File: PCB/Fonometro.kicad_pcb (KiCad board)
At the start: 2 copper layers, 120 x 120 mm, 58 parts, among them J1 Conn_01x15_Male, J2 Conn_01x15_Male, J3 Power, U1 LM324, U2 LM358, U3 ESP32-DEVKIT-V1

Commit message: feat: improved PCB layout.
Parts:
- added G***: LOGO, Logos:Jugg, F.Cu at (161.3, 127.0)
- added G***: LOGO, Logos:UniCT, F.Cu at (147.3, 127.0)
- moved R22 51.7 mm to (106.7, 120.6), turned to 90 degrees
- moved R23 41.6 mm to (124.5, 113.0), turned to -90 degrees
- moved U1 41.3 mm to (111.8, 104.1), turned to 0 degrees
- moved R21 36.9 mm to (106.7, 110.5)
- moved D2 36.9 mm to (177.8, 101.6), turned to 180 degrees
- moved D1 35.8 mm to (170.2, 106.7), turned to 0 degrees
- moved D4 29.5 mm to (177.8, 91.4), turned to 180 degrees
- moved R24 28.2 mm to (124.5, 101.6), turned to -90 degrees
- moved D3 24.1 mm to (170.2, 96.5), turned to 0 degrees
- moved R29 14.0 mm to (133.3, 68.6)
- moved J3 11.3 mm to (188.0, 79.5), turned to 120 degrees
- moved R30 11.2 mm to (121.1, 59.3), turned to 35 degrees
- moved U2 10.9 mm to (133.4, 62.2)
- moved C3 8.89 mm to (189.2, 116.8)
- moved R5 8.89 mm to (189.2, 110.5)
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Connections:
- R22 pad 1: Net-(R18-Pad2) -> MIC 2
- R22 pad 2: MIC 2 -> Net-(R18-Pad2)
- R24 pad 1: Net-(R20-Pad2) -> MIC 4
- R24 pad 2: MIC 4 -> Net-(R20-Pad2)
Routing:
- added copper zone on B.Cu, net GND
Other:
- board size 120 x 120 mm -> 100 x 100 mm
- board text added: "JLCJLCJLCJLC"
- board text added: "University of Catania, Italy DIY ESP32 Sound Meter By Davide Scalisi Rev. 1.0"

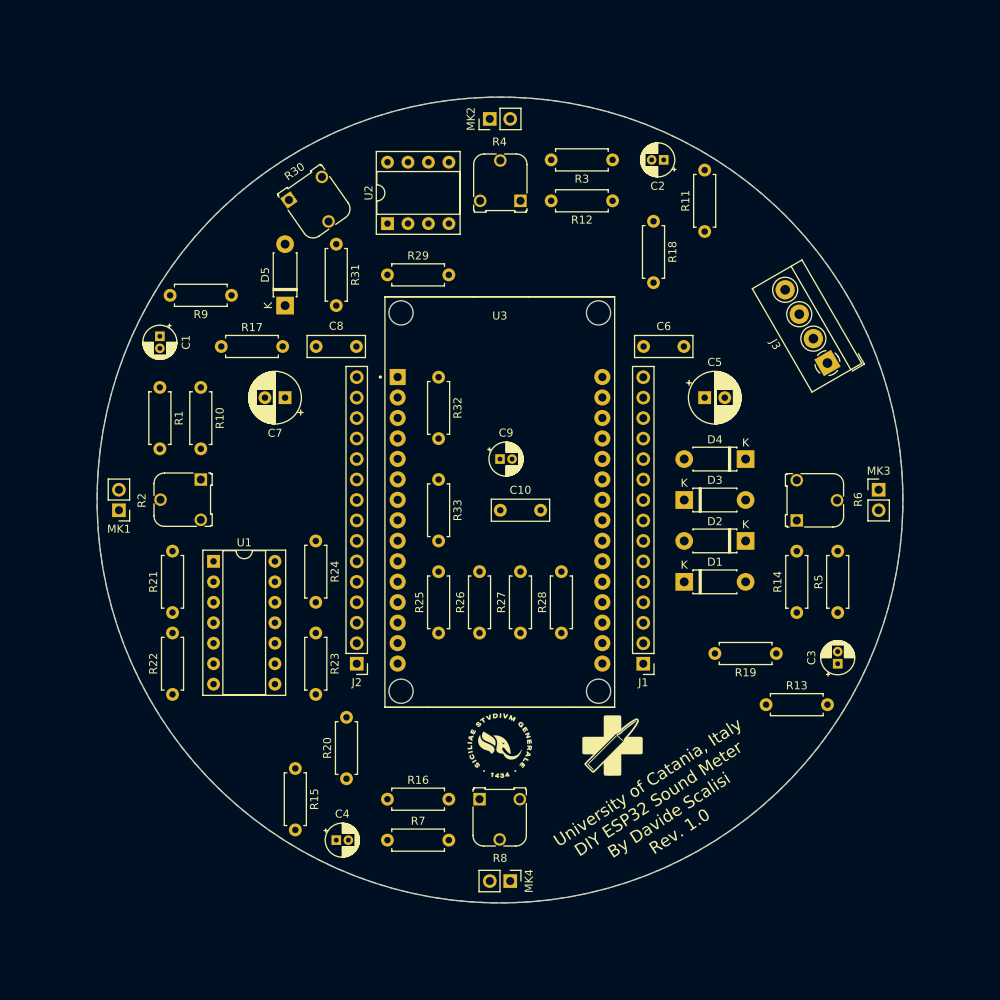
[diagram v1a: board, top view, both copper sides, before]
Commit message: feat: added single channel ADC input on MCU.
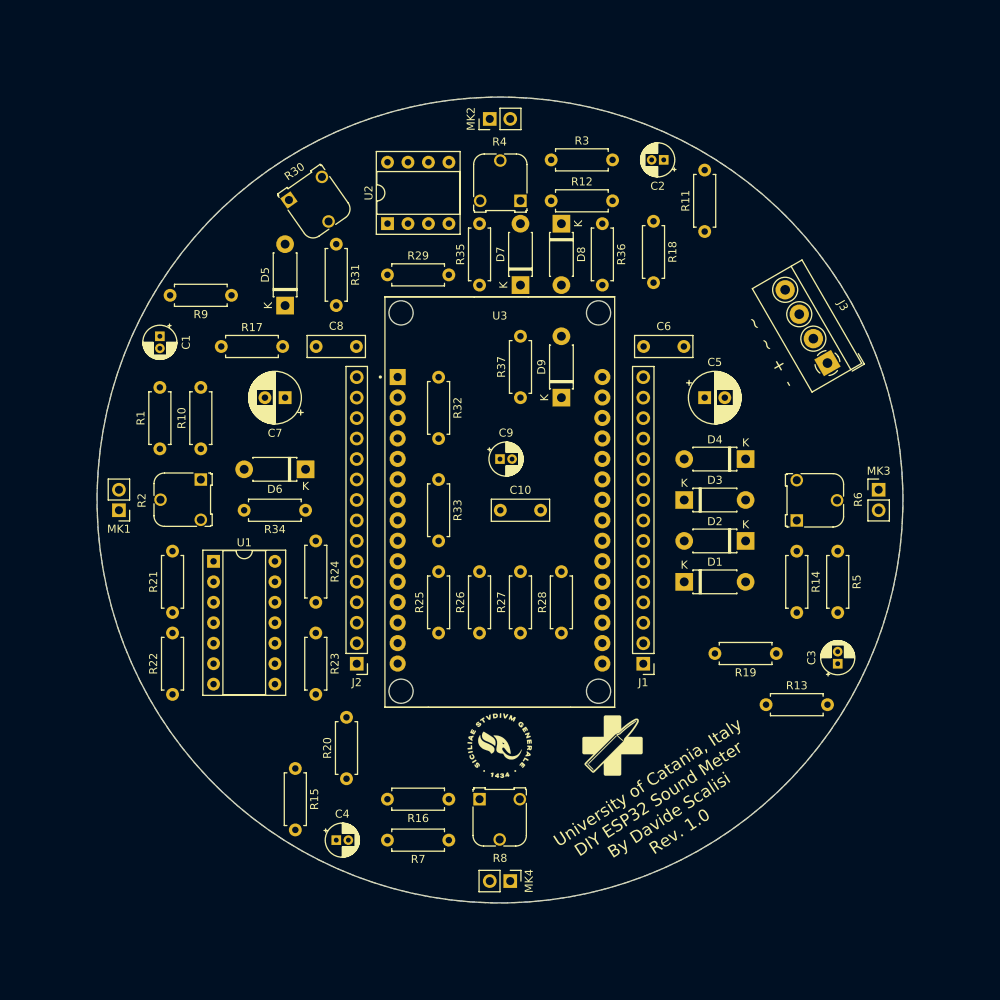
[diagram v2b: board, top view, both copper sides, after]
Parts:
- added D6: 3.3V, Diode_THT:D_DO-41_SOD81_P7.62mm_Horizontal, F.Cu at (123.2, 92.7)
- added D7: 3.3V, Diode_THT:D_DO-41_SOD81_P7.62mm_Horizontal, F.Cu at (149.9, 69.8)
- added D8: 3.3V, Diode_THT:D_DO-41_SOD81_P7.62mm_Horizontal, F.Cu at (154.9, 62.2)
- added D9: 3.3V, Diode_THT:D_DO-41_SOD81_P7.62mm_Horizontal, F.Cu at (154.9, 83.8)
- added R34: 1k, Resistor_THT:R_Axial_DIN0207_L6.3mm_D2.5mm_P7.62mm_Horizontal, F.Cu at (123.2, 97.8)
- added R35: 1k, Resistor_THT:R_Axial_DIN0207_L6.3mm_D2.5mm_P7.62mm_Horizontal, F.Cu at (144.8, 69.8)
- added R36: 1k, Resistor_THT:R_Axial_DIN0207_L6.3mm_D2.5mm_P7.62mm_Horizontal, F.Cu at (160.0, 62.2)
- added R37: 1k, Resistor_THT:R_Axial_DIN0207_L6.3mm_D2.5mm_P7.62mm_Horizontal, F.Cu at (149.9, 83.8)
- R31: value 330 -> 1k
- moved R1 7.62 mm to (105.1, 90.2), turned to 90 degrees
- moved R10 7.62 mm to (110.2, 90.2), turned to 90 degrees
- moved R12 7.62 mm to (153.7, 59.4), turned to 0 degrees
- moved R16 7.62 mm to (141.0, 133.7), turned to 180 degrees
- moved R3 7.62 mm to (153.7, 54.3), turned to 0 degrees
- moved R7 7.62 mm to (141.0, 138.7), turned to 180 degrees
- moved R14 7.62 mm to (184.2, 102.9), turned to -90 degrees
- moved R5 7.62 mm to (189.2, 102.9), turned to -90 degrees
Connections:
- net VN renamed D39
- net VP renamed D36
- D5 pad 1: D34 -> D32
- R1 pad 1: +3V3 -> Net-(R2-Pad1)
- R1 pad 2: Net-(R1-Pad2) -> +3V3
- R10 pad 1: Net-(C1-Pad1) -> GND
- R10 pad 2: GND -> Net-(C1-Pad1)
- R12 pad 1: Net-(C2-Pad1) -> GND
- R12 pad 2: GND -> Net-(C2-Pad1)
- R14 pad 1: Net-(C3-Pad1) -> GND
- R14 pad 2: GND -> Net-(C3-Pad1)
- R16 pad 1: Net-(C4-Pad1) -> GND
- R16 pad 2: GND -> Net-(C4-Pad1)
- R2 pad 1: Net-(R1-Pad2) -> Net-(R2-Pad1)
- R3 pad 1: +3V3 -> Net-(R4-Pad1)
- R3 pad 2: Net-(R3-Pad2) -> +3V3
- R31 pad 2: D34 -> D32
- R4 pad 1: Net-(R3-Pad2) -> Net-(R4-Pad1)
- R5 pad 1: +3V3 -> Net-(R6-Pad1)
- R5 pad 2: Net-(R5-Pad2) -> +3V3
- R6 pad 1: Net-(R5-Pad2) -> Net-(R6-Pad1)
- R7 pad 1: +3V3 -> Net-(R8-Pad1)
- R7 pad 2: Net-(R7-Pad2) -> +3V3
- R8 pad 1: Net-(R7-Pad2) -> Net-(R8-Pad1)
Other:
- board text added: "~ ~ + -"

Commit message: feat: first working PCB release.
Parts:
- moved C9 50.6 mm to (115.6, 130.8)
- moved C10 43.8 mm to (113.1, 125.1)
- moved D8 9.16 mm to (160.0, 69.8), turned to 90 degrees
- moved R36 9.16 mm to (154.9, 69.8), turned to 90 degrees
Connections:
- R2 pad 3: (no net) -> Net-(C1-Pad2)
- R30 pad 3: (no net) -> Net-(R30-Pad2)
- R4 pad 3: (no net) -> Net-(C2-Pad2)
- R6 pad 3: (no net) -> Net-(C3-Pad2)
- R8 pad 3: (no net) -> Net-(C4-Pad2)
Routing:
- net +3V3: track 0.00 -> 282.5 mm
- net VCC: track 0.00 -> 205.0 mm
- net Net-(R18-Pad2): track 0.00 -> 113.5 mm, vias 0 -> 1
- net 1.65V: track 0.00 -> 109.4 mm
- net MIC 2: track 0.00 -> 105.6 mm, vias 0 -> 2
- net MIC 3: track 0.00 -> 105.3 mm, vias 0 -> 1
- net MIC 4: track 0.00 -> 102.4 mm, vias 0 -> 1
- net Net-(R19-Pad2): track 0.00 -> 74.7 mm, vias 0 -> 1
- net D32: track 0.00 -> 69.9 mm, vias 0 -> 2
- net D36: track 0.00 -> 69.1 mm, vias 0 -> 2
- net MIC 1: track 0.00 -> 68.3 mm, vias 0 -> 1
- net D39: track 0.00 -> 65.8 mm
- net Net-(R25-Pad2): track 0.00 -> 64.3 mm
- net D34: track 0.00 -> 51.8 mm, vias 0 -> 1
- net Net-(R17-Pad2): track 0.00 -> 42.8 mm
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
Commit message: fix
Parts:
- moved D7 0.25 mm to (149.9, 70.1)
- moved D8 0.25 mm to (160.0, 70.1)
- moved R35 0.25 mm to (144.8, 70.1)
- moved R36 0.25 mm to (154.9, 70.1)
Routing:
- net D34: track 51.8 -> 52.6 mm
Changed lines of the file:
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@@
       (outputformat 1)
       (mirror false)
-      (drillshape 1)
+      (drillshape 0)
       (scaleselection 1)
-      (outputdirectory "")
+      (outputdirectory "C:/Users/lozio/Desktop/Fonometro/")
     )
   )
@@
   (net 58 "Net-(R8-Pad1)")
   (footprint "Resistor_THT:R_Axial_DIN0207_L6.3mm_D2.5mm_P7.62mm_Horizontal" (layer "F.Cu")
-    (at 154.94 69.85 90)
+    (at 154.94 70.104 90)
     (descr "Resistor, Axial_DIN0207 series, Axial, Horizontal, pin pitch=7.62mm, 0.25W = 1/4W, length*diameter=6.3*2.5mm^2, http://cdn-reichelt.de/documents/datenblatt/B400/1_4W%23YAG.pdf")
     (tags "Resistor Axial_DIN0207 series Axial Horizontal pin pitch 7.62mm 0.25W = 1/4W length 6.3mm diameter 2.5mm")
@@
   )
   (footprint "Resistor_THT:R_Axial_DIN0207_L6.3mm_D2.5mm_P7.62mm_Horizontal" (layer "F.Cu")
-    (at 144.78 69.85 90)
+    (at 144.78 70.104 90)
     (descr "Resistor, Axial_DIN0207 series, Axial, Horizontal, pin pitch=7.62mm, 0.25W = 1/4W, length*diameter=6.3*2.5mm^2, http://cdn-reichelt.de/documents/datenblatt/B400/1_4W%23YAG.pdf")
     (tags "Resistor Axial_DIN0207 series Axial Horizontal pin pitch 7.62mm 0.25W = 1/4W length 6.3mm diameter 2.5mm")
@@
   )
   (footprint "Diode_THT:D_DO-41_SOD81_P7.62mm_Horizontal" (layer "F.Cu")
-    (at 160.02 69.85 90)
+    (at 160.02 70.104 90)
     (descr "Diode, DO-41_SOD81 series, Axial, Horizontal, pin pitch=7.62mm, , length*diameter=5.2*2.7mm^2, , http://www.diodes.com/_files/packages/DO-41%20(Plastic).pdf")
     (tags "Diode DO-41_SOD81 series Axial Horizontal pin pitch 7.62mm  length 5.2mm diameter 2.7mm")
@@
   )
   (footprint "Diode_THT:D_DO-41_SOD81_P7.62mm_Horizontal" (layer "F.Cu")
-    (at 149.86 69.85 90)
+    (at 149.86 70.104 90)
     (descr "Diode, DO-41_SOD81 series, Axial, Horizontal, pin pitch=7.62mm, , length*diameter=5.2*2.7mm^2, , http://www.diodes.com/_files/packages/DO-41%20(Plastic).pdf")
     (tags "Diode DO-41_SOD81 series Axial Horizontal pin pitch 7.62mm  length 5.2mm diameter 2.7mm")
@@
   (segment (start 177.8 91.44) (end 177.8 96.52) (width 0.508) (layer "F.Cu") (net 14))
   (segment (start 182.708398 70.433367) (end 177.8 75.341765) (width 0.508) (layer "F.Cu") (net 14))
-  (segment (start 154.94 69.85) (end 157.48 69.85) (width 0.254) (layer "F.Cu") (net 15))
   (segment (start 156.013786 87.191214) (end 157.48 85.725) (width 0.254) (layer "F.Cu") (net 15))
-  (segment (start 157.48 85.725) (end 157.48 69.85) (width 0.254) (layer "F.Cu") (net 15))
+  (segment (start 154.94 70.104) (end 160.02 70.104) (width 0.254) (layer "F.Cu") (net 15))
+  (segment (start 154.94 72.39) (end 154.94 70.104) (width 0.254) (layer "F.Cu") (net 15))
   (segment (start 156.013786 101.796214) (end 156.013786 87.191214) (width 0.254) (layer "F.Cu") (net 15))
   (segment (start 165.079 109.199) (end 165.1 109.22) (width 1.016) (layer "F.Cu") (net 15))
-  (segment (start 157.48 69.85) (end 160.02 69.85) (width 0.254) (layer "F.Cu") (net 15))
+  (segment (start 157.48 74.93) (end 154.94 72.39) (width 0.254) (layer "F.Cu") (net 15))
   (segment (start 160.02 109.199) (end 165.079 109.199) (width 1.016) (layer "F.Cu") (net 15))
+  (segment (start 157.48 85.725) (end 157.48 74.93) (width 0.254) (layer "F.Cu") (net 15))
   (via (at 156.013786 101.796214) (size 0.8) (drill 0.4) (layers "F.Cu" "B.Cu") (net 15))
   (segment (start 160.02 109.199) (end 157.48 106.659) (width 0.254) (layer "B.Cu") (net 15))
@@
   (segment (start 114.3 121.92) (end 114.3 121.905) (width 0.254) (layer "B.Cu") (net 46))
   (segment (start 142.875 73.66) (end 142.24 74.295) (width 0.254) (layer "B.Cu") (net 46))
+  (segment (start 152.781 62.484) (end 152.4 62.865) (width 0.254) (layer "F.Cu") (net 47))
+  (segment (start 152.4 62.865) (end 152.4 74.295) (width 0.254) (layer "F.Cu") (net 47))
   (segment (start 121.28 119.375) (end 122.555 120.65) (width 0.254) (layer "F.Cu") (net 47))
+  (segment (start 147.176511 75.073489) (end 146.246214 76.003786) (width 0.254) (layer "F.Cu") (net 47))
   (segment (start 122.56 120.645) (end 124.46 120.645) (width 0.254) (layer "F.Cu") (net 47))
+  (segment (start 152.4 74.295) (end 151.621511 75.073489) (width 0.254) (layer "F.Cu") (net 47))
   (segment (start 151.621511 75.073489) (end 147.176511 75.073489) (width 0.254) (layer "F.Cu") (net 47))
-  (segment (start 153.035 62.23) (end 152.4 62.865) (width 0.254) (layer "F.Cu") (net 47))
-  (segment (start 154.94 62.23) (end 153.035 62.23) (width 0.254) (layer "F.Cu") (net 47))
-  (segment (start 146.685 75.565) (end 146.246214 76.003786) (width 0.254) (layer "F.Cu") (net 47))
+  (segment (start 154.94 62.484) (end 152.781 62.484) (width 0.254) (layer "F.Cu") (net 47))
   (segment (start 122.555 120.65) (end 122.56 120.645) (width 0.254) (layer "F.Cu") (net 47))
   (segment (start 119.39 119.375) (end 121.28 119.375) (width 0.254) (layer "F.Cu") (net 47))
-  (segment (start 147.176511 75.073489) (end 146.685 75.565) (width 0.254) (layer "F.Cu") (net 47))
   (segment (start 146.246214 76.003786) (end 146.246214 102.673786) (width 0.254) (layer "F.Cu") (net 47))
-  (segment (start 152.4 62.865) (end 152.4 74.295) (width 0.254) (layer "F.Cu") (net 47))
-  (segment (start 152.4 74.295) (end 151.621511 75.073489) (width 0.254) (layer "F.Cu") (net 47))
   (via (at 146.246214 102.673786) (size 0.8) (drill 0.4) (layers "F.Cu" "B.Cu") (net 47))
   (segment (start 124.46 121.273128) (end 128.281872 125.095) (width 0.254) (layer "B.Cu") (net 47))

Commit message: feat: J4 and J5 for U2B.
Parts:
- added J4: Conn_01x05_Female, Connector_PinHeader_2.54mm:PinHeader_1x05_P2.54mm_Vertical, F.Cu at (130.8, 51.4)
- added J5: Conn_01x01_Female, Connector_PinHeader_2.54mm:PinHeader_1x01_P2.54mm_Vertical, F.Cu at (129.5, 55.2)
- moved U2 0.63 mm to (133.4, 62.9)
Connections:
- R2 pad 3: Net-(C1-Pad2) -> (no net)
- R30 pad 3: Net-(R30-Pad2) -> (no net)
- R4 pad 3: Net-(C2-Pad2) -> (no net)
- R6 pad 3: Net-(C3-Pad2) -> (no net)
- R8 pad 3: Net-(C4-Pad2) -> (no net)
- U2 pad 5: unconnected-(U2-Pad5) -> Net-(J4-Pad5)
- U2 pad 6: unconnected-(U2-Pad6) -> Net-(U2-Pad6)
- U2 pad 7: unconnected-(U2-Pad7) -> Net-(J4-Pad3)
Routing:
- net +3V3: track 282.5 -> 289.0 mm
- net Net-(J4-Pad5): track 0.00 -> 3.81 mm
- net Net-(U2-Pad6): track 0.00 -> 3.81 mm
- net Net-(J4-Pad3): track 0.00 -> 3.80 mm
- net VCC: track 205.0 -> 208.2 mm
- net Net-(R18-Pad2): track 113.5 -> 111.4 mm
- net Net-(R30-Pad2): track 18.8 -> 18.1 mm
- net Net-(R25-Pad2): track 64.3 -> 63.7 mm

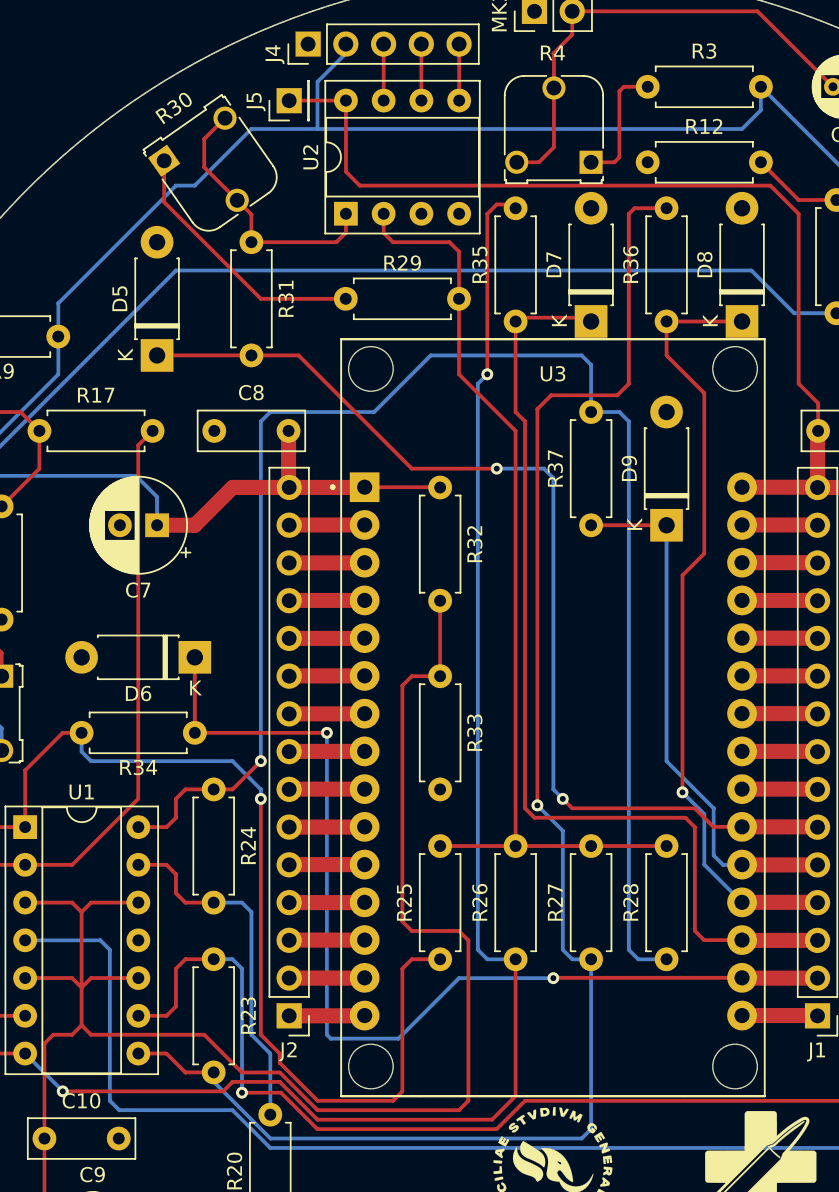
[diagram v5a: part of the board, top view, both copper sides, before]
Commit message: fix: now U2A.+ is connected to 1.65V.
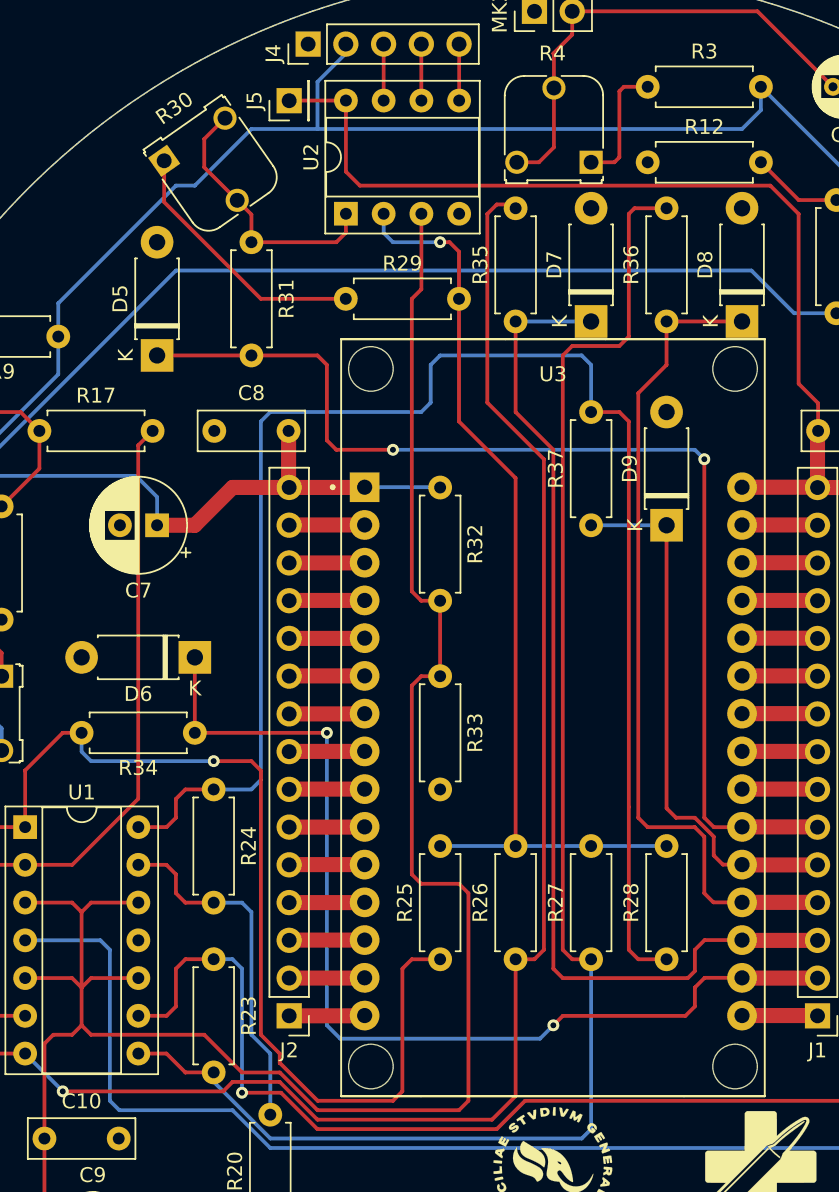
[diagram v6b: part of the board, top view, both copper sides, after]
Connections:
- R2 pad 3: (no net) -> Net-(C1-Pad2)
- R30 pad 3: (no net) -> Net-(R30-Pad2)
- R4 pad 3: (no net) -> Net-(C2-Pad2)
- R6 pad 3: (no net) -> Net-(C3-Pad2)
- R8 pad 3: (no net) -> Net-(C4-Pad2)
- U2 pad 3: GND -> 1.65V
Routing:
- net 1.65V: track 109.4 -> 136.0 mm
- net D32: track 69.9 -> 74.7 mm
- net D39: track 65.8 -> 69.6 mm
- net D34: track 52.6 -> 55.9 mm, vias 1 -> 0
- net MIC 4: track 102.4 -> 104.6 mm, vias 1 -> 0
- net MIC 3: track 105.2 -> 103.0 mm, vias 1 -> 0
- net MIC 1: track 68.3 -> 69.0 mm
- net D35: track 35.9 -> 36.6 mm
- net MIC 2: track 105.6 -> 106.3 mm, vias 2 -> 1
- net Net-(R25-Pad2): vias 0 -> 1
